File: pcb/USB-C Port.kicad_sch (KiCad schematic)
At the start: 8 parts, among them J3 USB_C_Receptacle_USB2.0_16P, U2 USBLC6-2SC6

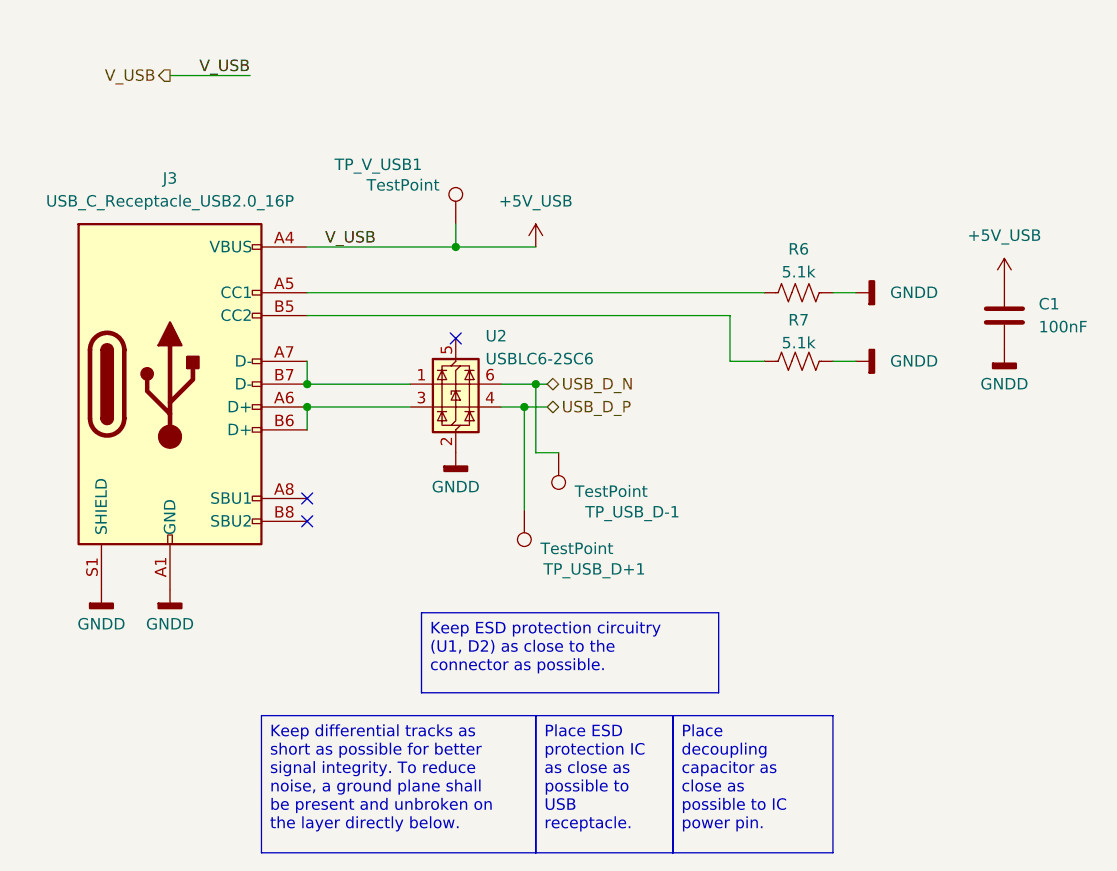
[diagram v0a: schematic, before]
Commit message: Updated schematics and removed most test points
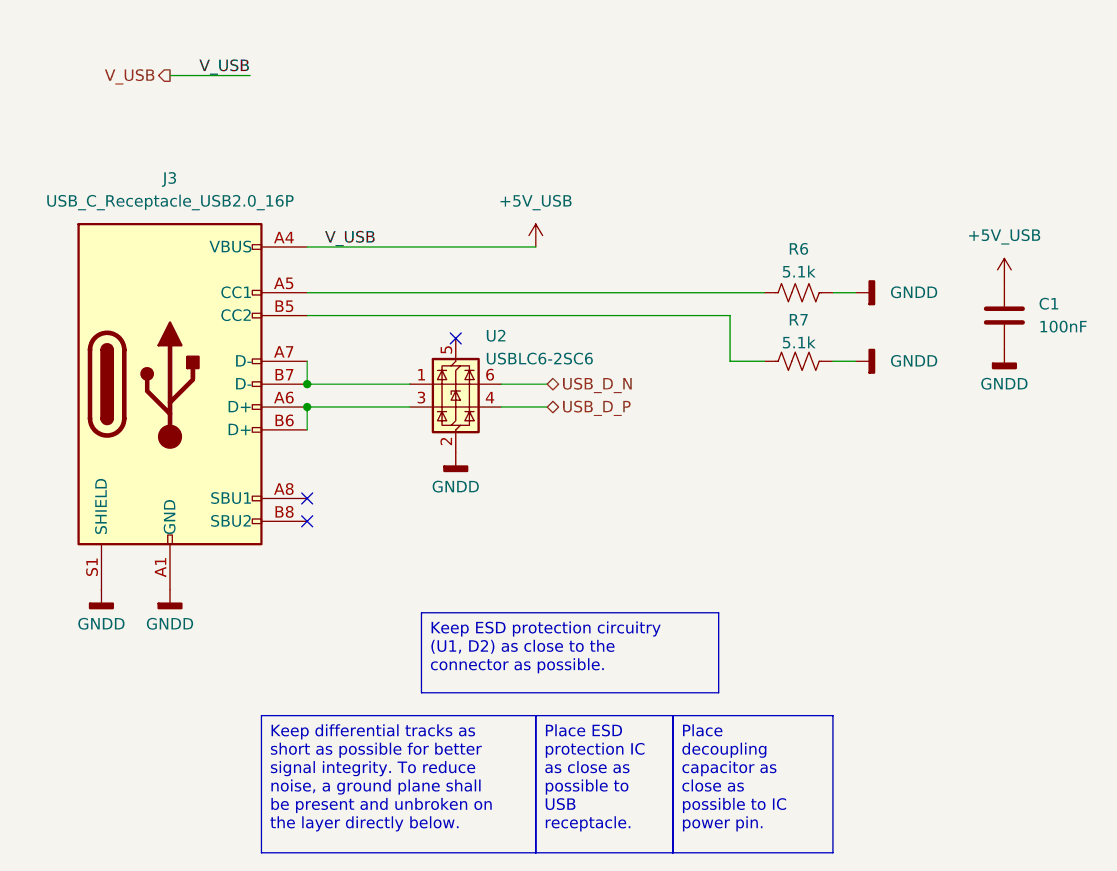
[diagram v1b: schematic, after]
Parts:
- removed TP_USB_D+1, TP_USB_D-1, TP_V_USB1: TestPoint, TestPoint:TestPoint_Loop_D2.54mm_Drill1.5mm_Beaded, symbol Connector:TestPoint
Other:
- title: Ride-Along Module -> Control Module Rev2

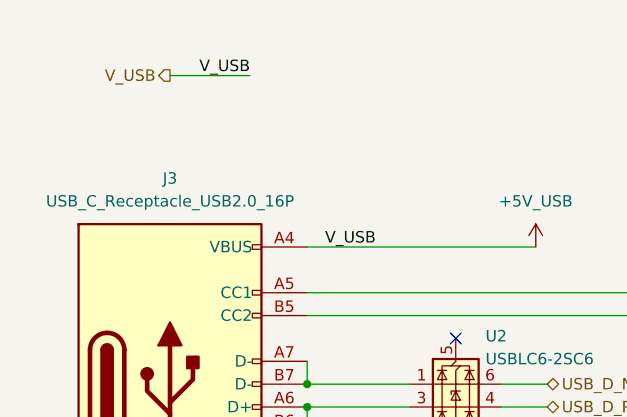
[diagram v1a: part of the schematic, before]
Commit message: Updated Board size and layout
Full Layout of Rev 2 board, without RF shield and other updates.
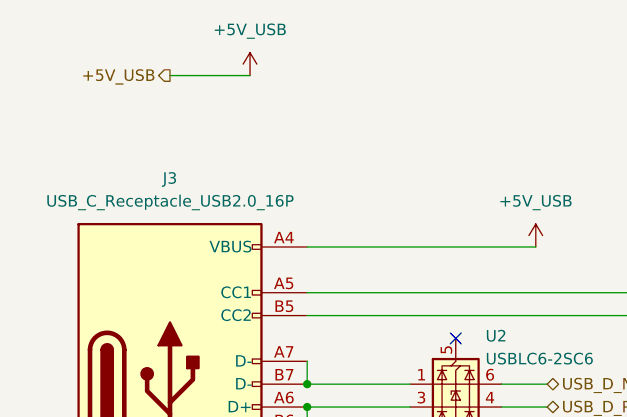
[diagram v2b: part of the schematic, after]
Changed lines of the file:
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@@
-		)
-	)
-	(label "V_USB"
-		(at 69.85 62.23 180)
-		(effects
-			(font
-				(size 1.27 1.27)
-			)
-			(justify right bottom)
-		)
-	)
-	(label "V_USB"
-		(at 55.88 43.18 180)
-		(effects
-			(font
-				(size 1.27 1.27)
-			)
-			(justify right bottom)
 		)
 	)
@@
 		)
 	)
-	(hierarchical_label "V_USB"
+	(hierarchical_label "+5V_USB"
 		(shape output)
 		(at 46.99 43.18 180)
@@
 					(unit 1)
 				)
+			)
+		)
+	)
+	(symbol
+		(lib_id "power:+5V")
+		(at 55.88 43.18 0)
+		(unit 1)
+		(exclude_from_sim no)
+		(in_bom yes)
+		(on_board yes)
+		(dnp no)
+		(fields_autoplaced yes)
+		(property "Reference" "#PWR0123"
+			(at 55.88 46.99 0)
+			(effects
+				(font
+					(size 1.27 1.27)
+				)
+				(hide yes)
+			)
+		)
+		(property "Value" "+5V_USB"
+			(at 55.88 38.1 0)
+			(effects
+				(font
+					(size 1.27 1.27)
+				)
+			)
+		)
+		(property "Footprint" ""
+			(at 55.88 43.18 0)
+			(effects
+				(font
+					(size 1.27 1.27)
+				)
+				(hide yes)
+			)
+		)
+		(property "Datasheet" ""
+			(at 55.88 43.18 0)
+			(effects
+				(font
+					(size 1.27 1.27)
+				)
+				(hide yes)
+			)
+		)
+		(property "Description" "Power symbol creates a global label with name \"+5V\""
+			(at 55.88 43.18 0)
+			(effects
+				(font
+					(size 1.27 1.27)
+				)
+				(hide yes)
+			)
+		)
+		(pin "1"
+		)
+		(instances
+			(project "control-module"
+				(path "/ba7b4294-8d75-4b9e-892f-fb52727887ec/b41619a2-11a0-4fcf-9c2d-b1ec93f6b99c"
+					(reference "#PWR0123")
+					(unit 1)
+				)
